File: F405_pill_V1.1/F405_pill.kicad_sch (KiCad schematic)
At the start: 49 parts, among them J1 Conn_01x04_Male, J2 Conn_01x04_Male, J4 TYPE-C-31-M-12, U1 STM32F405RGTx, U2 TJA1050T/CM,118, U3 LM1117-3.3, U4 STM32F405_pill, U5 HT7550, Y1 Crystal_GND24

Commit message: add imu
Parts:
- added J5: Conn_01x02, Connector_PinHeader_2.54mm:PinHeader_1x02_P2.54mm_Vertical, symbol Connector_Generic:Conn_01x02
- added R91 (x2): 2.4K, Resistor_SMD:R_0805_2012Metric, symbol Device:R
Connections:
- net +3V3: now also R91.1, R91.2
- net DUAL1: no longer U1.29 (PB10)
- net DUAL2: no longer U1.30 (PB11)
- new net PB10: J5.1 (Pin_1), R91.2, U1.29 (PB10)
- new net PB11: J5.2 (Pin_2), R91.1, U1.30 (PB11)
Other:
- added sheet imu (imu.kicad_sch)

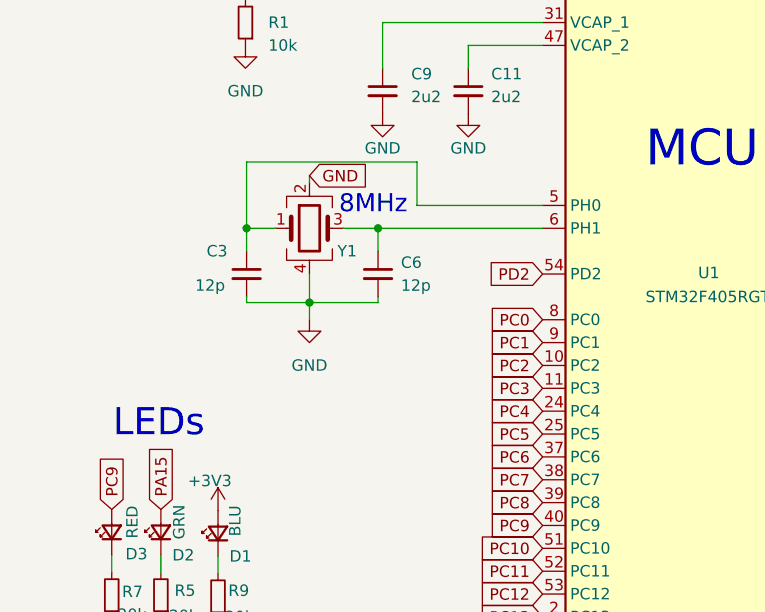
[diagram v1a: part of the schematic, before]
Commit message: fixed for prodaction
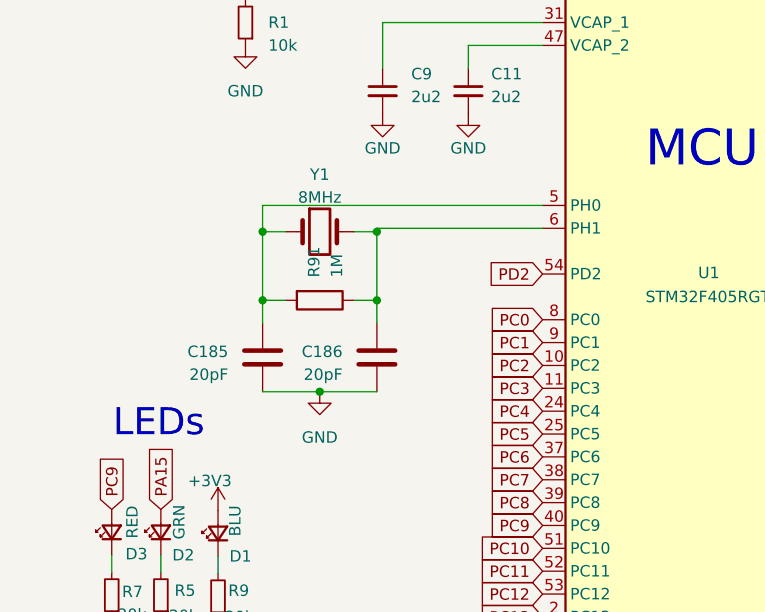
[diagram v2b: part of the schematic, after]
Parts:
- removed C3, C6: 12p, Capacitor_SMD:C_0402_1005Metric, symbol Device:C_Small
- removed Y1: Crystal_GND24, Crystal:Crystal_SMD_3225-4Pin_3.2x2.5mm, symbol Device:Crystal_GND24
- added C185, C186: 20pF, Capacitor_SMD:C_0402_1005Metric, symbol Device:C
- added R91: 1M, Resistor_SMD:R_0402_1005Metric, symbol Device:R
- added Y1: 8MHz, Crystal:Crystal_SMD_5032-2Pin_5.0x3.2mm, symbol Device:Crystal
- R10, R11: LCSC C105872 -> C25905
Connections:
- net GND: now also C185.1, C186.1
- net at U1.6 (PH1): now also C186.2, R91.1, Y1.2
- net at U1.5 (PH0): now also C185.2, R91.2, Y1.1
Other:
- note removed: "8MHz"

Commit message: add MCU
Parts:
- removed U1: STM32F405RGTx, Package_QFP:LQFP-64_10x10mm_P0.5mm, symbol MCU_ST_STM32F4:STM32F405RGTx
- added U1: STM32F405VGTx, Package_QFP:LQFP-100_14x14mm_P0.5mm, symbol MCU_ST_STM32F4:STM32F405VGTx
- U2: value TJA1050T/CM,118 -> TJA1050T/CM,118
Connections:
- net +3.3VA: now also U1.21 (VREF+), U1.22 (VDDA)
- net +3V3: now also U1.100 (VDD), U1.11 (VDD), U1.19 (VDD), U1.28 (VDD), U1.50 (VDD), U1.6 (VBAT), U1.75 (VDD)
- net GND: now also U1.10 (VSS), U1.20 (VSSA), U1.27 (VSS), U1.37 (PB2), U1.74 (VSS), U1.99 (VSS)
- net NRST: now also U1.14 (NRST)
- net PA0: now also U1.23 (PA0)
- net PA1: now also U1.24 (PA1)
- net PA10: now also U1.69 (PA10)
- net PA15: now also U1.77 (PA15)
- net PA2: now also U1.25 (PA2)
- net PA3: now also U1.26 (PA3)
- net PA4: now also U1.29 (PA4)
- net PA5: now also U1.30 (PA5)
- net PA6: now also U1.31 (PA6)
- net PA7: now also U1.32 (PA7)
- net PA8: now also U1.67 (PA8)
- net PA9: now also U1.68 (PA9)
- net PB0: now also U1.35 (PB0)
- net PB1: now also U1.36 (PB1)
- net PB10: now also U1.47 (PB10)
- net PB11: now also U1.48 (PB11)
- net PB12: now also U1.51 (PB12)
- net PB13: now also U1.52 (PB13)
- net PB14: now also U1.53 (PB14)
- net PB15: now also U1.54 (PB15)
- net PB3: now also U1.89 (PB3)
- net PB4: now also U1.90 (PB4)
- net PB5: now also U1.91 (PB5)
- net PB6: now also U1.92 (PB6)
- net PB7: now also U1.93 (PB7)
- net PB8: now also U1.95 (PB8)
- net PB9: now also U1.96 (PB9)
- net PC0: now also U1.15 (PC0)
- net PC1: now also U1.16 (PC1)
- net PC10: now also U1.78 (PC10)
- net PC11: now also U1.79 (PC11)
- net PC12: now also U1.80 (PC12)
- net PC13: now also U1.7 (PC13)
- net PC14: now also U1.8 (PC14)
- net PC15: now also U1.9 (PC15)
- net PC2: now also U1.17 (PC2)
- net PC3: now also U1.18 (PC3)
- net PC4: now also U1.33 (PC4)
- net PC5: now also U1.34 (PC5)
- net PC6: now also U1.63 (PC6)
- net PC7: now also U1.64 (PC7)
- net PC8: now also U1.65 (PC8)
- net PC9: now also U1.66 (PC9)
- net SWCLK: now also U1.76 (PA14)
- net SWDIO: now also U1.72 (PA13)
- net USB_D+: now also U1.71 (PA12)
- net USB_D-: now also U1.70 (PA11)
- net at JP1.2 (B), R1.2: now also U1.94 (BOOT0)
- net at C186.2, R91.1, Y1.2: now also U1.13 (PH1)
- net at C185.2, R91.2, Y1.1: now also U1.12 (PH0)
- net at C9.1: now also U1.49 (VCAP_1)
- net at C11.1: now also U1.73 (VCAP_2)
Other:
- note removed: "MCU"
- moved on the sheet: C1, C10, C11, C12, C13, C14, C15, C16, C17, C18, C185, C186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

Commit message: Schematic is finished
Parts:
- renumbered R91 to R133, R91 to R54
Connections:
- net NRF/TX: now reaches U1.85 (PD4)
- net NRF/RX: now reaches U1.86 (PD5)
- net PA0 renamed A_PHA_VSENSE
- net PA1 renamed A_PHB_VSENSE
- net PA10 renamed HIN_C
- net PA2 renamed A_PHC_VSENSE
- net PA4 renamed A_THROTTLE
- net PA8 renamed HIN_A
- net PA9 renamed HIN_B
- net PB1 renamed FET_TEMP
- net PB10 renamed I2C_SCL
- net PB11 renamed I2C_SDA
- net PB13 renamed LIN_A
- net PB14 renamed LIN_B
- net PB15 renamed LIN_C
- net PC0 renamed A_SHA_AMP
- net PC1 renamed A_SHB_AMP
- net PC2 renamed A_SHC_AMP
- net PC3 renamed VSENSE
- net PC6 renamed HALL_C
- net PC7 renamed HALL_B
- net PC8 renamed HALL_A
- net _PB12 renamed A_OVERLIMIT
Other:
- added sheet NRF (nrf.kicad_sch)
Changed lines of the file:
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@@
 	(wire
 		(pts
+			(xy 120.65 168.91) (xy 142.24 168.91)
+		)
+		(stroke
+			(width 0)
+			(type default)
+		)
+	)
+	(wire
+		(pts
 			(xy 327.66 232.41) (xy 342.9 232.41)
 		)
@@
 	(wire
 		(pts
+			(xy 120.65 171.45) (xy 142.24 171.45)
+		)
+		(stroke
+			(width 0)
+			(type default)
+		)
+	)
+	(wire
+		(pts
 			(xy 370.84 224.79) (xy 368.3 224.79)
 		)
@@
 	(text "NC\nGND\nV3V3\nADC SPI1SCK DAC TIM2\nADC SPI1MISO TIM3\nJP3 / FET TEMP\nA_PHC_VSENSE\nJP2 / MOTOR TEMP / SPI1MOSI\nA_PHB_VSENSE\nA_PHA_VSENSE\nA_SHC_AMP\nA_SHB_AMP\nA_SHA_AMP\nVSENSE\nA_THROTTLE\nJP3 / FET TEMP\nHALL_C\nHALL_B\nHALL_A\nNC"
 		(exclude_from_sim no)
-		(at 359.918 76.073 0)
+		(at 367.03 75.692 0)
 		(effects
 			(font
@@
 	(text "A_OVERLIMIT\nLIN_A\nLIB_B\nLIB_C\nHIN_A\nHIN_B\nHIN_C\nTX3 SCL2 + ADC\nRX3 SDA2 + ADC\nSCK3 TX4\nMISO3 TIM3 RX4\nMOSI3, TIM3 CANRX\nTIM4 TX1 SCL1 CANTX\nRX1 SDA1 TIM4\nSPI3 MOSI / GPIO\nSPI3 MISO RX4\nSPI3 SCK TX4\nV5V\nGND\nV3V3"
 		(exclude_from_sim no)
-		(at 313.436 75.692 0)
+		(at 308.356 75.692 0)
 		(effects
 			(font
@@
 		)
 	)
-	(global_label "PA0"
+	(global_label "A_PHA_VSENSE"
 		(shape input)
 		(at 187.96 92.71 0)
@@
 		)
 	)
-	(global_label "PA9"
+	(global_label "HIN_B"
 		(shape input)
 		(at 322.58 39.37 180)
@@
 		)
 	)
-	(global_label "PA4"
+	(global_label "A_THROTTLE"
 		(shape input)
 		(at 350.52 62.23 0)
@@
 		)
 	)
-	(global_label "PB15"
+	(global_label "LIN_C"
 		(shape input)
 		(at 322.58 34.29 180)
@@
 		)
 	)
-	(global_label "PC8"
+	(global_label "HALL_A"
 		(shape input)
 		(at 350.52 72.39 0)
@@
 		)
 	)
-	(global_label "PA2"
+	(global_label "A_PHC_VSENSE"
 		(shape input)
 		(at 387.096 99.568 180)
@@
 		)
 	)
-	(global_label "PA2"
+	(global_label "A_PHC_VSENSE"
 		(shape input)
 		(at 187.96 97.79 0)
@@
 		)
 	)
-	(global_label "PB13"
+	(global_label "LIN_A"
 		(shape input)
 		(at 187.96 168.91 0)
@@
 		)
 	)
-	(global_label "PC2"
+	(global_label "A_SHC_AMP"
 		(shape input)
 		(at 350.52 52.07 0)
@@
 		)
 	)
-	(global_label "PA4"
+	(global_label "A_THROTTLE"
 		(shape input)
 		(at 187.96 102.87 0)
@@
 		)
 	)
-	(global_label "PC1"
+	(global_label "A_SHB_AMP"
 		(shape input)
 		(at 187.96 181.61 0)
@@
 		)
 	)
-	(global_label "PC8"
+	(global_label "HALL_A"
 		(shape input)
 		(at 187.96 199.39 0)
@@
 		)
 	)
-	(global_label "PA8"
+	(global_label "HIN_A"
 		(shape input)
 		(at 187.96 113.03 0)
@@
 		)
 	)
-	(global_label "PB14"
+	(global_label "LIN_B"
 		(shape input)
 		(at 322.58 31.75 180)
@@
 		)
 	)
-	(global_label "PC7"
+	(global_label "HALL_B"
 		(shape input)
 		(at 350.52 69.85 0)
@@
 		)
 	)
-	(global_label "PC2"
+	(global_label "A_SHC_AMP"
 		(shape input)
 		(at 187.96 184.15 0)
@@
 		)
 	)
-	(global_label "PA0"
+	(global_label "A_PHA_VSENSE"
 		(shape input)
 		(at 350.52 49.53 0)
@@
 		)
 	)
-	(global_label "PC7"
+	(global_label "HALL_B"
 		(shape input)
 		(at 187.96 196.85 0)
@@
 		)
 	)
-	(global_label "PB11"
+	(global_label "I2C_SDA"
 		(shape input)
 		(at 370.84 138.43 0)
@@
 		)
 		(property "Intersheetrefs" "${INTERSHEET_REFS}"
-			(at 378.7842 138.43 0)
+			(at 381.4452 138.43 0)
 			(effects
 				(font
@@
 		)
 	)
-	(global_label "_PB12"
+	(global_label "A_OVERLIMIT"
 		(shape input)
 		(at 347.98 88.773 180)
@@
 		)
 	)
-	(global_label "PB15"
+	(global_label "LIN_C"
 		(shape input)
 		(at 187.96 173.99 0)
@@
 		)
 	)
-	(global_label "PB1"
+	(global_label "FET_TEMP"
 		(shape input)
 		(at 187.96 138.43 0)
@@
 		)
 		(property "Intersheetrefs" "${INTERSHEET_REFS}"
-			(at 194.1226 138.3506 0)
+			(at 199.956 138.43 0)
 			(effects
 				(font
@@
 		)
 	)
-	(global_label "PA1"
+	(global_label "A_PHB_VSENSE"
 		(shape input)
 		(at 387.35 87.503 180)
@@
 		)
 	)
-	(global_label "PB10"
+	(global_label "I2C_SCL"
 		(shape input)
 		(at 372.11 135.89 0)
@@
 		)
 		(property "Intersheetrefs" "${INTERSHEET_REFS}"
-			(at 380.0542 135.89 0)
+			(at 382.6547 135.89 0)
 			(effects
 				(font
@@
 		)
 	)
-	(global_label "PA8"
+	(global_label "HIN_A"
 		(shape input)
 		(at 322.58 36.83 180)
@@
 		)
 	)
-	(global_label "PB10"
+	(global_label "I2C_SCL"
 		(shape input)
 		(at 187.96 161.29 0)
@@
 		)
 		(property "Intersheetrefs" "${INTERSHEET_REFS}"
-			(at 195.3321 161.2106 0)
+			(at 198.5047 161.29 0)
 			(effects
 				(font
@@
 		)
 	)
-	(global_label "PC1"
+	(global_label "A_SHB_AMP"
 		(shape input)
 		(at 350.52 54.61 0)
@@
 		)
 	)
-	(global_label "PA10"
+	(global_label "HIN_C"
 		(shape input)
 		(at 187.96 118.11 0)
@@
 		)
 	)
-	(global_label "PB14"
+	(global_label "LIN_B"
 		(shape input)
 		(at 187.96 171.45 0)
@@
 		)
 	)
-	(global_label "_PB12"
+	(global_label "A_OVERLIMIT"
 		(shape input)
 		(at 322.58 26.67 180)
@@
 		)
 	)
-	(global_label "PA9"
+	(global_label "HIN_B"
 		(shape input)
 		(at 187.96 115.57 0)
@@
 		)
 	)
-	(global_label "PC3"
+	(global_label "VSENSE"
 		(shape input)
 		(at 350.52 59.69 0)
@@
 		)
 	)
-	(global_label "PC0"
+	(global_label "A_SHA_AMP"
 		(shape input)
 		(at 350.52 57.15 0)
@@
 		)
 	)
-	(global_label "PB11"
+	(global_label "I2C_SDA"
 		(shape input)
 		(at 187.96 163.83 0)
@@
 		)
 		(property "Intersheetrefs" "${INTERSHEET_REFS}"
-			(at 195.3321 163.7506 0)
+			(at 198.5652 163.83 0)
 			(effects
 				(font
@@
 		)
 	)
-	(global_label "PA2"
+	(global_label "A_PHC_VSENSE"
 		(shape input)
 		(at 350.52 41.91 0)
@@
 		)
 	)
-	(global_label "PA0"
+	(global_label "A_PHA_VSENSE"
 		(shape input)
 		(at 387.731 75.184 180)
@@
 		)
 	)
-	(global_label "PB1"
+	(global_label "FET_TEMP"
 		(shape input)
 		(at 350.52 39.37 0)
@@
 		)
 	)
-	(global_label "PC6"
+	(global_label "HALL_C"
 		(shape input)
 		(at 187.96 194.31 0)
@@
 		)
 	)
-	(global_label "PB13"
+	(global_label "LIN_A"
 		(shape input)
 		(at 322.58 29.21 180)
@@
 		)
 	)
-	(global_label "PA1"
+	(global_label "A_PHB_VSENSE"
 		(shape input)
 		(at 187.96 95.25 0)
@@
 		)
 	)
-	(global_label "PC6"
+	(global_label "HALL_C"
 		(shape input)
 		(at 350.52 67.31 0)
@@
 		)
 	)
-	(global_label "PC3"
+	(global_label "VSENSE"
 		(shape input)
 		(at 187.96 186.69 0)
@@
 		)
 	)
-	(global_label "PC0"
+	(global_label "A_SHA_AMP"
 		(shape input)
 		(at 187.96 179.07 0)
@@
 		)
 	)
-	(global_label "PA1"
+	(global_label "A_PHB_VSENSE"
 		(shape input)
 		(at 350.52 46.99 0)
@@
 		)
 	)
-	(global_label "PA10"
+	(global_label "HIN_C"
 		(shape input)
 		(at 322.58 41.91 180)
@@
 		(dnp no)
 		(fields_autoplaced yes)
-		(property "Reference" "R91"
+		(property "Reference" "R133"
 			(at 122.555 115.57 0)
 			(effects
@@
 		(dnp no)
 		(fields_autoplaced yes)
-		(property "Reference" "R91"
+		(property "Reference" "R54"
 			(at 368.3 129.54 0)
 			(effects
@@
 		(dnp no)
 		(fields_autoplaced yes)
-		(property "Reference" "R91"
+		(property "Reference" "R54"
 			(at 364.49 124.46 0)
 			(effects
@@
 				)
 			)
+		)
+	)
+	(sheet
+		(at 107.95 167.64)
+		(size 12.7 5.08)
+		(fields_autoplaced yes)
+		(stroke
+			(width 0.1524)
+			(type solid)
+		)
+		(fill
+			(color 0 0 0 0.0000)
+		)
+		(property "Sheetname" "NRF"
+			(at 107.95 166.9284 0)
+			(effects
+				(font
+					(size 1.27 1.27)
+				)
+				(justify left bottom)
+			)
+		)
+		(property "Sheetfile" "nrf.kicad_sch"
+			(at 107.95 173.3046 0)
+			(effects
+				(font
+					(size 1.27 1.27)
+				)
+				(justify left top)
+			)
+		)
+		(pin "RX" input
+			(at 120.65 171.45 0)
+			(effects
+				(font
+					(size 1.27 1.27)
+				)
+				(justify right)
+			)
+		)
+		(pin "TX" input
+			(at 120.65 168.91 0)
+			(effects
+				(font
+					(size 1.27 1.27)
+				)
+				(justify right)
+			)
+		)
+		(instances
+			(project "F405_pill"
+				(path "/e63e39d7-6ac0-4ffd-8aa3-1841a4541b55"
+					(page "3")
+				)
+			)

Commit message: Fixed pin
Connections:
- net NRF/TX: now also U1.87 (PD6); no longer U1.85 (PD4)
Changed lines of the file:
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@@
 	(wire
 		(pts
-			(xy 313.69 223.52) (xy 313.69 231.14)
+			(xy 120.65 173.99) (xy 142.24 173.99)
 		)
 		(stroke
@@
 	(wire
 		(pts
-			(xy 109.22 97.79) (xy 142.24 97.79)
+			(xy 313.69 223.52) (xy 313.69 231.14)
 		)
 		(stroke
@@
 	(wire
 		(pts
-			(xy 120.65 168.91) (xy 142.24 168.91)
+			(xy 109.22 97.79) (xy 142.24 97.79)
 		)
 		(stroke
@@
 	)
 	(sheet
-		(at 107.95 167.64)
+		(at 107.95 170.18)
 		(size 12.7 5.08)
 		(fields_autoplaced yes)
@@
 		)
 		(property "Sheetname" "NRF"
-			(at 107.95 166.9284 0)
+			(at 107.95 169.4684 0)
 			(effects
 				(font
@@
 		)
 		(property "Sheetfile" "nrf.kicad_sch"
-			(at 107.95 173.3046 0)
+			(at 107.95 175.8446 0)
 			(effects
 				(font
@@
 		)
 		(pin "TX" input
-			(at 120.65 168.91 0)
+			(at 120.65 173.99 0)
 			(effects
 				(font

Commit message: updated for prodaction
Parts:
- removed U3: LM1117-3.3, Package_TO_SOT_SMD:SOT-223-3_TabPin2, symbol Regulator_Linear:LM1117-3.3
- added U7: AMS1117-3.3, Package_TO_SOT_SMD:SOT-223-3_TabPin2, symbol Regulator_Linear:AMS1117-3.3
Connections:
- net +3V3: now also U7.2 (VO)
- net +5V: now also U7.3 (VI)
- net GND: now also U7.1 (GND)
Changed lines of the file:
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@@
-	)
-	(symbol
-		(lib_id "Regulator_Linear:LM1117-3.3")
-		(at 378.46 224.79 0)
-		(unit 1)
-		(exclude_from_sim no)
-		(in_bom yes)
-		(on_board yes)
-		(dnp no)
-		(fields_autoplaced yes)
-		(property "Reference" "U3"
-			(at 378.46 217.17 0)
-			(effects
-				(font
-					(size 1.27 1.27)
-				)
-				(hide yes)
-			)
-		)
-		(property "Value" "LM1117-3.3"
-			(at 378.46 220.218 0)
-			(effects
-				(font
-					(size 1.27 1.27)
-				)
-			)
-		)
-		(property "Footprint" "Package_TO_SOT_SMD:SOT-223-3_TabPin2"
-			(at 378.46 224.79 0)
-			(effects
-				(font
-					(size 1.27 1.27)
-				)
-				(hide yes)
-			)
-		)
-		(property "Datasheet" "https://datasheet.lcsc.com/lcsc/1811131822_HTC-Korea-TAEJIN-Tech-LM1117S-3-3_C126027.pdf"
-			(at 378.46 224.79 0)
-			(effects
-				(font
-					(size 1.27 1.27)
-				)
-				(hide yes)
-			)
-		)
-		(property "Description" ""
-			(at 378.46 224.79 0)
-			(effects
-				(font
-					(size 1.27 1.27)
-				)
-				(hide yes)
-			)
-		)
-		(property "LCSC" "C126027"
-			(at 378.46 224.79 0)
-			(effects
-				(font
-					(size 1.27 1.27)
-				)
-				(hide yes)
-			)
-		)
-		(pin "1"
-		)
-		(pin "2"
-		)
-		(pin "3"
-		)
-		(instances
-			(project "F405_pill"
-				(path "/e63e39d7-6ac0-4ffd-8aa3-1841a4541b55"
-					(reference "U3")
-					(unit 1)
-				)
-			)
-		)
 	)
 	(symbol
@@
 					(unit 1)
 				)
+			)
+		)
+	)
+	(symbol
+		(lib_id "Regulator_Linear:AMS1117-3.3")
+		(at 378.46 224.79 0)
+		(unit 1)
+		(exclude_from_sim no)
+		(in_bom yes)
+		(on_board yes)
+		(dnp no)
+		(fields_autoplaced yes)
+		(property "Reference" "U7"
+			(at 378.46 218.44 0)
+			(effects
+				(font
+					(size 1.27 1.27)
+				)
+			)
+		)
+		(property "Value" "AMS1117-3.3"
+			(at 378.46 220.98 0)
+			(effects
+				(font
+					(size 1.27 1.27)
+				)
+			)
+		)
+		(property "Footprint" "Package_TO_SOT_SMD:SOT-223-3_TabPin2"
+			(at 378.46 219.71 0)
+			(effects
+				(font
+					(size 1.27 1.27)
+				)
+				(hide yes)
+			)
+		)
+		(property "Datasheet" "http://www.advanced-monolithic.com/pdf/ds1117.pdf"
+			(at 381 231.14 0)
+			(effects
+				(font
+					(size 1.27 1.27)
+				)
+				(hide yes)
+			)
+		)
+		(property "Description" "1A Low Dropout regulator, positive, 3.3V fixed output, SOT-223"
+			(at 378.46 224.79 0)
+			(effects
+				(font
+					(size 1.27 1.27)
+				)
+				(hide yes)
+			)
+		)
+		(property "MPN" "C6186"
+			(at 378.46 224.79 0)
+			(effects
+				(font
+					(size 1.27 1.27)
+				)
+				(hide yes)
+			)
+		)
+		(pin "3"
+		)
+		(pin "2"
+		)
+		(pin "1"
+		)
+		(instances
+			(project ""
+				(path "/e63e39d7-6ac0-4ffd-8aa3-1841a4541b55"
+					(reference "U7")
+					(unit 1)
+				)
